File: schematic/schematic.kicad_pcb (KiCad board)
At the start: 2 copper layers, 53 parts, among them J1 USB_C_Receptacle_USB2.0, J2 Battery Connector, J3 Peltier Connection, SW1 SW_DIP_x01, U1 MC34063AD, U2 IRS2103, U3 MCP73832-2-OT, U4 BUK9K52-60E, U5 BUK9K52-60E, U6 IRS2103, U7 ESP32-D-WD-V3, Y1 Crystal_GND24

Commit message: schematic done
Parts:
- removed C9: 4.64pF, Capacitor_SMD:C_0805_2012Metric_Pad1.18x1.45mm_HandSolder
- added J4: Serial, Connector_PinHeader_2.54mm:PinHeader_1x03_P2.54mm_Vertical, F.Cu at (71.4, 97.7)
- added R20: 90k, Resistor_SMD:R_0805_2012Metric_Pad1.20x1.40mm_HandSolder, F.Cu at (94.0, 127.9)
- added R21: 90k, Resistor_SMD:R_0805_2012Metric_Pad1.20x1.40mm_HandSolder, F.Cu at (98.7, 124.9)
- added R24: 90k, Resistor_SMD:R_0805_2012Metric_Pad1.20x1.40mm_HandSolder, F.Cu at (103.5, 124.9)
- added TH1: SDNT2012X103F3950FTF, Resistor_SMD:R_0805_2012Metric_Pad1.20x1.40mm_HandSolder, F.Cu at (98.7, 130.8)
- added TH2: SDNT2012X103F3950FTF, Resistor_SMD:R_0805_2012Metric_Pad1.20x1.40mm_HandSolder, F.Cu at (103.5, 127.9)
- added TH3: SDNT2012X103F3950FTF, Resistor_SMD:R_0805_2012Metric_Pad1.20x1.40mm_HandSolder, F.Cu at (103.5, 130.8)
- C1: value 100pF -> 3.797pF
- C10: value 3.3nF -> 100nF; moved to B.Cu
- C11: value 10nF -> 10uF; moved to B.Cu
- C12: value 100nF -> 10uF; moved to B.Cu
- C13: value 10pF -> 10uF; moved to B.Cu
- C14, U4: moved to B.Cu
- C15: value 10pF -> 100pF; moved to B.Cu
- C16: value 100nF -> 100uF; footprint Capacitor_SMD:C_0805_2012Metric_Pad1.18x1.45mm_HandSolder -> Capacitor_SMD:C_1210_3225Metric_Pad1.33x2.70mm_HandSolder
- C18: value 100nF -> 1uF
- C2: value 100uF -> 4.64pF; footprint Capacitor_SMD:C_1206_3216Metric_Pad1.33x1.80mm_HandSolder -> Capacitor_SMD:C_0805_2012Metric_Pad1.18x1.45mm_HandSolder
- C3: value 10uF -> 3.3nF; moved to B.Cu
- C4: value 10uF -> 10nF; moved to B.Cu
- C5: value 1uF -> 100nF; moved to B.Cu
- C6: value 100nF -> 10pF; moved to B.Cu
- C7: value 10uF -> 10pF; moved to B.Cu
- C8: value 3.797pF -> 100nF
- D1, D2: value 1N5819 -> STPS130U; footprint Diode_THT:D_DO-41_SOD81_P10.16mm_Horizontal -> Diode_SMD:D_SMB; moved to B.Cu
- D3: value LED -> STPS130U; footprint Diode_THT:D_DO-41_SOD81_P10.16mm_Horizontal -> Diode_SMD:D_SMB
- D4: value 1N5819 -> LED; footprint Diode_THT:D_DO-41_SOD81_P10.16mm_Horizontal -> LED_SMD:LED_0805_2012Metric_Pad1.15x1.40mm_HandSolder; moved to B.Cu
- J1: value USB_C_Receptacle_USB2.0 -> Battery Connector; footprint 1KicadLib:USB4125-GF-A -> Connector_PinHeader_2.54mm:PinHeader_1x02_P2.54mm_Vertical
- J2: value Battery Connector -> USB_C_Receptacle_USB2.0; footprint Connector_PinHeader_2.54mm:PinHeader_1x02_P2.54mm_Vertical -> 1KicadLib:USB4125-GF-A
- L1: value 150uH -> 1.807nH; footprint Inductor_SMD:L_6.3x6.3_H3 -> Inductor_SMD:L_0805_2012Metric_Pad1.15x1.40mm_HandSolder
- L2: value 1.807nH -> 150uH; footprint Inductor_SMD:L_0805_2012Metric_Pad1.15x1.40mm_HandSolder -> Inductor_SMD:L_6.3x6.3_H3
- R1: value .22 -> 20k
- R10: value 470 -> .22; moved to B.Cu
- R11: value 10k -> 180
- R12: value 10k -> 500; moved to B.Cu
- R13: value 20k -> 3.6k; moved to B.Cu
- R14: value 10k -> 2.2k; moved to B.Cu
- R15: value 10k -> 470; moved to B.Cu
- R2, R3: value 0 -> 10k
- R4: value 180 -> 10k
- R5: value 5.1k -> 10k; footprint Capacitor_SMD:C_0805_2012Metric_Pad1.18x1.45mm_HandSolder -> Resistor_SMD:R_0805_2012Metric_Pad1.20x1.40mm_HandSolder
- R6: value 5.1k -> 76k; footprint Capacitor_SMD:C_0805_2012Metric_Pad1.18x1.45mm_HandSolder -> Resistor_SMD:R_0805_2012Metric_Pad1.20x1.40mm_HandSolder
- R7: value 3.6k -> 24k
- R8: value 2.2k -> 5.1k; footprint Resistor_SMD:R_0805_2012Metric_Pad1.20x1.40mm_HandSolder -> Capacitor_SMD:C_0805_2012Metric_Pad1.18x1.45mm_HandSolder; moved to B.Cu
- R9: value 2k -> 5.1k; footprint Resistor_SMD:R_0805_2012Metric_Pad1.20x1.40mm_HandSolder -> Capacitor_SMD:C_0805_2012Metric_Pad1.18x1.45mm_HandSolder; moved to B.Cu
- U1: value MC34063AD -> ESP32-D-WD-V3; footprint Package_SO:SOIC-8_3.9x4.9mm_P1.27mm -> Package_DFN_QFN:QFN-48-1EP_5x5mm_P0.35mm_EP3.7x3.7mm_ThermalVias
- U3: value MCP73832-2-OT -> BUK9K52-60E; footprint Package_TO_SOT_SMD:SOT-23-5 -> 1KicadLib:LFPAK56D; moved to B.Cu
- U5: value BUK9K52-60E -> IRS2103; footprint 1KicadLib:LFPAK56D -> Package_SO:SOIC-8_3.9x4.9mm_P1.27mm
- U6: value IRS2103 -> MC34063AD; moved to B.Cu
- U7: value ESP32-D-WD-V3 -> TP4054; footprint Package_DFN_QFN:QFN-48-1EP_5x5mm_P0.35mm_EP3.7x3.7mm_ThermalVias -> Package_TO_SOT_SMD:SOT-23-5_HandSoldering
- moved C3 68.1 mm to (79.6, 102.4), turned to 270 degrees
- moved C6 63.8 mm to (77.4, 98.8), turned to 180 degrees
- moved R12 63.3 mm to (82.2, 91.2), turned to 90 degrees
- moved R15 61.5 mm to (83.9, 90.9), turned to 270 degrees
- moved C10 60.5 mm to (80.9, 96.9), turned to 90 degrees
- moved R1 55.6 mm to (79.6, 102.3), turned to 270 degrees
- moved AE1 53.6 mm to (81.9, 117.1), turned to 270 degrees
- moved C5 52.8 mm to (83.2, 102.2)
- moved R11 52.5 mm to (88.4, 93.4), turned to 90 degrees
- moved R7 52.2 mm to (87.9, 102.5), turned to 270 degrees
- moved R8 51.8 mm to (94.3, 87.2), turned to 90 degrees
- moved R10 50.7 mm to (86.1, 94.7), turned to 270 degrees
- moved R14 50.2 mm to (90.3, 98.7)
- moved C7 49.3 mm to (77.2, 95.8)
- moved R13 49.2 mm to (87.1, 99.6), turned to 90 degrees
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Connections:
- C1 pad 1: Net-(C1-Pad1) -> Net-(AE1-Pad1)
- C10 pad 1: Net-(C10-Pad1) -> +3V3
- C10 pad 2: Net-(C10-Pad2) -> GND
- C11 pad 1: Net-(C10-Pad2) -> VCC_UNREGULATED
- C12 pad 1: +3V3 -> Net-(C12-Pad1)
- C12 pad 2: GND -> /Peltier Driver/PELTIER_P
- C13 pad 2: GND -> /Peltier Driver/PELTIER_N
- C14 pad 1: Net-(C14-Pad1) -> VCC_UNREGULATED
- C14 pad 2: Net-(C14-Pad2) -> GND
- C17 pad 1: +BATT -> +3V3
- C2 pad 1: +3V3 -> Net-(C2-Pad1)
- C3 pad 1: +BATT -> Net-(C3-Pad1)
- C3 pad 2: GND -> Net-(C3-Pad2)
- C4 pad 1: +3V3 -> Net-(C3-Pad2)
- C6 pad 1: +3V3 -> Net-(C6-Pad1)
- C7 pad 2: Net-(C7-Pad2) -> GND
- C8 pad 1: Net-(AE1-Pad1) -> +3V3
- D1 pad 1: Net-(D1-Pad1) -> Net-(C12-Pad1)
- D1 pad 2: GND -> VCC_UNREGULATED
- D2 pad 1: Net-(C7-Pad1) -> Net-(D2-Pad1)
- D2 pad 2: +BATT -> GND
- D3 pad 1: Net-(D3-Pad1) -> Net-(C13-Pad1)
- D3 pad 2: Net-(D3-Pad2) -> VCC_UNREGULATED
- D4 pad 1: Net-(C14-Pad1) -> Net-(D4-Pad1)
- D4 pad 2: +BATT -> Net-(D4-Pad2)
- J3 pad 1: Net-(C14-Pad2) -> /Peltier Driver/PELTIER_N
- J3 pad 2: Net-(C7-Pad2) -> /Peltier Driver/PELTIER_P
- L1 pad 1: +3V3 -> Net-(AE1-Pad1)
- L1 pad 2: Net-(D1-Pad1) -> Net-(C2-Pad1)
- L2 pad 1: Net-(AE1-Pad1) -> +3V3
- L2 pad 2: Net-(C9-Pad1) -> Net-(D2-Pad1)
- R1 pad 1: Net-(R1-Pad1) -> Net-(C3-Pad1)
- R1 pad 2: +BATT -> Net-(C3-Pad2)
- R10 pad 1: VBUS -> Net-(R10-Pad1)
- R10 pad 2: Net-(D3-Pad2) -> VCC_UNREGULATED
- R11 pad 1: Net-(R11-Pad1) -> Net-(R10-Pad1)
- R12 pad 1: Net-(R12-Pad1) -> GND
- R13 pad 1: Net-(C10-Pad1) -> +3V3
- R13 pad 2: Net-(C10-Pad2) -> Net-(R13-Pad2)
- R14 pad 1: Net-(R14-Pad1) -> Net-(R13-Pad2)
- R14 pad 2: Net-(R14-Pad2) -> GND
- R15 pad 1: Net-(R15-Pad1) -> VBUS
- R15 pad 2: Net-(R15-Pad2) -> Net-(D4-Pad2)
- R2 pad 1: Net-(J1-PadA6) -> Net-(R2-Pad1)
- R2 pad 2: TXD -> Net-(R2-Pad2)
- R3 pad 1: Net-(J1-PadA7) -> Net-(R3-Pad1)
- R3 pad 2: RXD -> Net-(R3-Pad2)
- R4 pad 1: Net-(R1-Pad1) -> Net-(R4-Pad1)
- R5 pad 1: Net-(J1-PadB5) -> Net-(R5-Pad1)
- R5 pad 2: GND -> Net-(R5-Pad2)
- R6 pad 1: Net-(J1-PadA5) -> VCC_UNREGULATED
- R6 pad 2: GND -> Net-(R6-Pad2)
- R7 pad 1: +3V3 -> Net-(R6-Pad2)
- R7 pad 2: Net-(R7-Pad2) -> GND
- R8 pad 1: Net-(R7-Pad2) -> Net-(J2-PadB5)
- R9 pad 1: GND -> Net-(J2-PadA5)
- R9 pad 2: Net-(R9-Pad2) -> GND
- SW1 pad 1: Net-(J2-Pad1) -> VCC_UNREGULATED
- SW1 pad 2: +BATT -> /Power Management/BATT_IN
- U1 pad 1: Net-(R1-Pad1) -> +3V3
- U1 pad 2: Net-(D1-Pad1) -> Net-(C2-Pad1)
- U1 pad 3: Net-(C1-Pad1) -> +3V3
- U1 pad 4: GND -> +3V3
- U1 pad 5: Net-(R7-Pad2) -> Net-(U1-Pad5)
- U1 pad 6: +BATT -> Net-(U1-Pad6)
- U1 pad 7: Net-(R1-Pad1) -> Net-(U1-Pad7)
- U1 pad 8: Net-(R4-Pad2) -> Net-(U1-Pad8)
- U2 pad 1: +BATT -> VCC_UNREGULATED
- U2 pad 2: HBridgeA -> DRIVER_P
- U2 pad 3: HBridgeA -> DRIVER_P
- U2 pad 5: Net-(R12-Pad2) -> Net-(R3-Pad2)
- U2 pad 6: Net-(C7-Pad2) -> /Peltier Driver/PELTIER_P
- U2 pad 7: Net-(R11-Pad2) -> Net-(R2-Pad2)
- U2 pad 8: Net-(C7-Pad1) -> Net-(C12-Pad1)
- U3 pad 1: Net-(D3-Pad1) -> /Peltier Driver/PELTIER_P
- U3 pad 2: GND -> Net-(R2-Pad1)
- U3 pad 3: Net-(J2-Pad1) -> GND
- U3 pad 4: VBUS -> Net-(R3-Pad1)
- U3 pad 5: Net-(R9-Pad2) -> /Peltier Driver/PELTIER_P
- U4 pad 1: Net-(C7-Pad2) -> /Peltier Driver/PELTIER_N
- U4 pad 2: Net-(R11-Pad1) -> Net-(R4-Pad1)
- U4 pad 4: Net-(R12-Pad1) -> Net-(R5-Pad1)
- U4 pad 5: Net-(C7-Pad2) -> /Peltier Driver/PELTIER_N
- U4 pad 6: Net-(C7-Pad2) -> /Peltier Driver/PELTIER_N
- U4 pad 7: +BATT -> VCC_UNREGULATED
- U4 pad 8: +BATT -> VCC_UNREGULATED
- U5 pad 1: Net-(C14-Pad2) -> VCC_UNREGULATED
- U5 pad 2: Net-(R14-Pad1) -> DRIVER_N
- U5 pad 3: GND -> DRIVER_N
- U5 pad 4: Net-(R15-Pad1) -> GND
- U5 pad 5: Net-(C14-Pad2) -> Net-(R5-Pad2)
- U5 pad 6: Net-(C14-Pad2) -> /Peltier Driver/PELTIER_N
- U5 pad 7: +BATT -> Net-(R4-Pad2)
- U5 pad 8: +BATT -> Net-(C13-Pad1)
- U6 pad 1: +BATT -> Net-(R10-Pad1)
- U6 pad 2: HBridgeB -> Net-(D2-Pad1)
- U6 pad 3: HBridgeB -> Net-(C15-Pad1)
- U6 pad 5: Net-(R15-Pad2) -> Net-(R13-Pad2)
- U6 pad 6: Net-(C14-Pad2) -> VCC_UNREGULATED
- U6 pad 7: Net-(R14-Pad2) -> Net-(R10-Pad1)
- U6 pad 8: Net-(C14-Pad1) -> Net-(R11-Pad2)
- U7 pad 1: +3V3 -> Net-(D4-Pad1)
- U7 pad 2: Net-(C9-Pad1) -> GND
- U7 pad 3: +3V3 -> /Power Management/BATT_IN
- U7 pad 4: +3V3 -> VBUS
- U7 pad 5: Net-(U7-Pad5) -> Net-(R12-Pad2)
- Y1 pad 1: Net-(C13-Pad1) -> Net-(C6-Pad1)
- Y1 pad 3: Net-(C15-Pad1) -> Net-(C7-Pad1)
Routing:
- net VCC_UNREGULATED: track 0.00 -> 81.1 mm, vias 0 -> 6
- net DRIVER_P: track 0.00 -> 48.3 mm, vias 0 -> 2
- net +3V3: track 0.00 -> 42.8 mm, vias 0 -> 5
- net DRIVER_N: track 0.00 -> 31.9 mm
- net /Peltier Driver/PELTIER_P: track 0.00 -> 31.4 mm, vias 0 -> 1
- net /Power Management/BATT_IN: track 0.00 -> 24.6 mm
- net /Peltier Driver/PELTIER_N: track 0.00 -> 23.7 mm, vias 0 -> 1
- net VBUS: track 0.00 -> 15.4 mm, vias 0 -> 2
- net GND: track 0.00 -> 11.8 mm, vias 0 -> 8
- net Net-(C2-Pad1): track 0.00 -> 8.32 mm
- net Net-(C7-Pad1): track 0.00 -> 8.06 mm, vias 0 -> 1
- net Net-(C12-Pad1): track 0.00 -> 8.04 mm, vias 0 -> 1
- net Net-(R10-Pad1): track 0.00 -> 7.81 mm, vias 0 -> 1
- net Net-(C13-Pad1): track 0.00 -> 7.33 mm, vias 0 -> 1
- net Net-(D2-Pad1): track 0.00 -> 5.75 mm
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- added copper zone on B.Cu, net GND
- added copper zone on F.Cu, net GND
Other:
- net class Default: clearance 0.2 -> 0.127; trace_width 0.25 -> 0.127; via_dia 0.8 -> 0.4; via_drill 0.4 -> 0.2
- rule trace_clearance: 0.2 -> 0.127
- rule trace_min: 0.2 -> 0.127
- rule via_min_drill: 0.3 -> 0.2

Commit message: nightly
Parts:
- removed J1: Battery Connector, Connector_PinHeader_2.54mm:PinHeader_1x02_P2.54mm_Vertical
- added Je: BATT, Connector_PinHeader_1.27mm:PinHeader_1x02_P1.27mm_Vertical, F.Cu at (137.4, 64.3)
- J3: value Peltier Connection -> Pelt; footprint Connector_PinHeader_2.54mm:PinHeader_1x02_P2.54mm_Vertical -> Connector_PinHeader_1.27mm:PinHeader_1x02_P1.27mm_Vertical
- J4: footprint Connector_PinHeader_2.54mm:PinHeader_1x03_P2.54mm_Vertical -> Connector_PinHeader_1.27mm:PinHeader_1x03_P1.27mm_Vertical
- SW1: value SW_DIP_x01 -> PS; footprint Connector_PinHeader_2.54mm:PinHeader_1x02_P2.54mm_Vertical -> Connector_PinHeader_1.27mm:PinHeader_1x02_P1.27mm_Vertical
- moved AE1 75.8 mm to (154.7, 95.8)
- moved C1 73.8 mm to (153.5, 91.9), turned to 45 degrees
- moved L1 71.9 mm to (150.9, 90.6), turned to 135 degrees
- moved C2 67.7 mm to (148.1, 89.3), turned to 225 degrees
- moved J4 67.2 mm to (137.3, 84.7), turned to 90 degrees
- moved SW1 64.6 mm to (137.3, 69.2)
- moved J3 64.4 mm to (172.6, 71.1)
- moved C4 64.1 mm to (138.0, 81.0)
- moved R13 64.1 mm to (147.6, 78.2)
- moved C7 64.1 mm to (137.7, 74.4)
- moved C8 64.1 mm to (148.3, 77.3)
- moved L2 64.1 mm to (153.5, 75.4)
- moved R12 64.1 mm to (142.6, 69.8)
- moved R3 64.1 mm to (164.1, 63.6)
- moved R6 64.1 mm to (150.2, 81.1)
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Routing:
- net +3V3: track 42.8 -> 138.6 mm, vias 5 -> 7
- net GND: track 11.8 -> 102.3 mm, vias 8 -> 28
- net TEMP_SENSE_3: track 0.00 -> 63.8 mm, vias 0 -> 2
- net TEMP_SENSE_2: track 0.00 -> 44.8 mm, vias 0 -> 2
- net TEMP_SENSE_1: track 0.00 -> 31.6 mm, vias 0 -> 2
- net RXD: track 0.00 -> 10.8 mm
- net TXD: track 0.00 -> 9.84 mm
- net /Power Management/BATT_IN: track 24.6 -> 17.1 mm, vias 0 -> 1
- net Net-(C2-Pad1): track 8.32 -> 13.0 mm
- net DRIVER_N: track 31.9 -> 34.9 mm
- net /Peltier Driver/PELTIER_N: track 23.7 -> 24.8 mm
- net DRIVER_P: track 48.3 -> 49.2 mm
- net Net-(AE1-Pad1): track 3.79 -> 4.48 mm
- net VCC_UNREGULATED: track 81.1 -> 80.6 mm
- net Net-(C7-Pad1): track 8.06 -> 7.82 mm, vias 1 -> 2
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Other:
- board outline added: 40.6 x 70.5 mm
- board text added: "GUANTANAMO BAY"
- board text added: "Joesphan Lu"

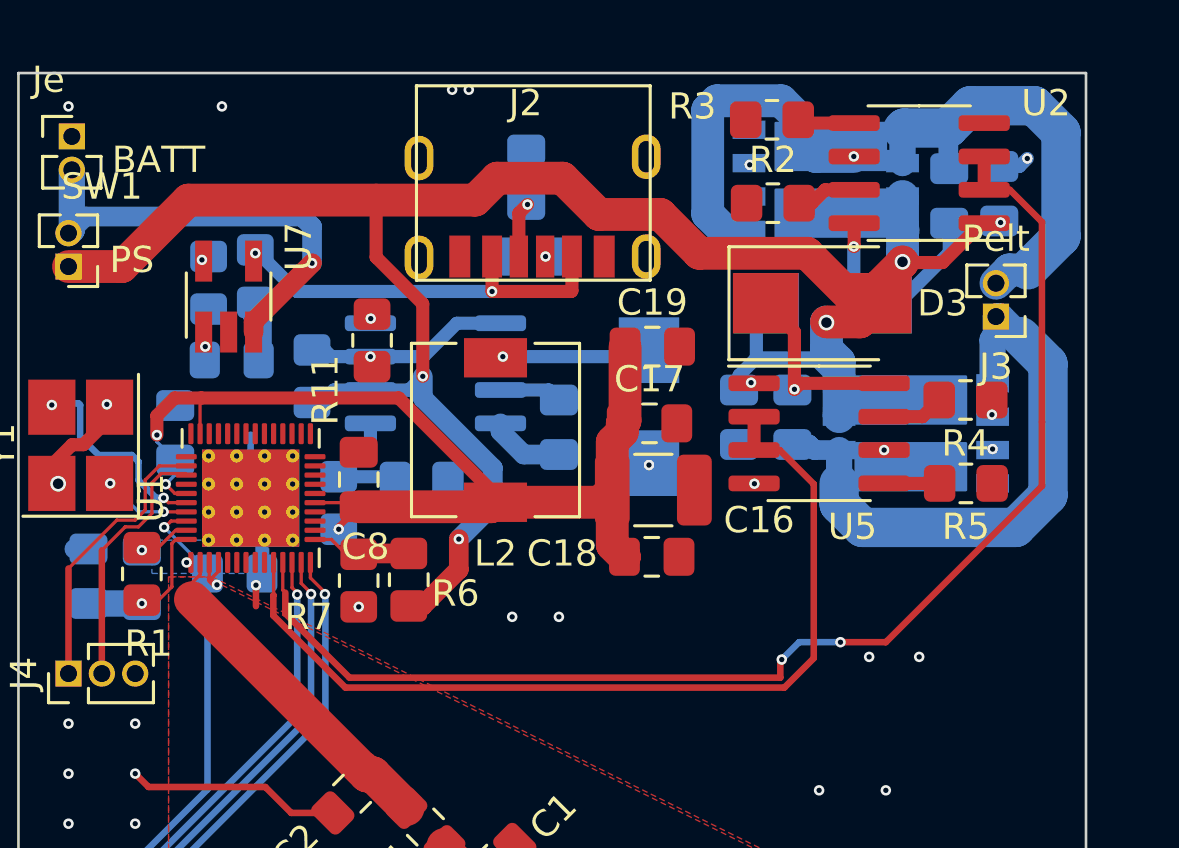
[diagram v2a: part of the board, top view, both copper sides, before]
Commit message: fixed vias
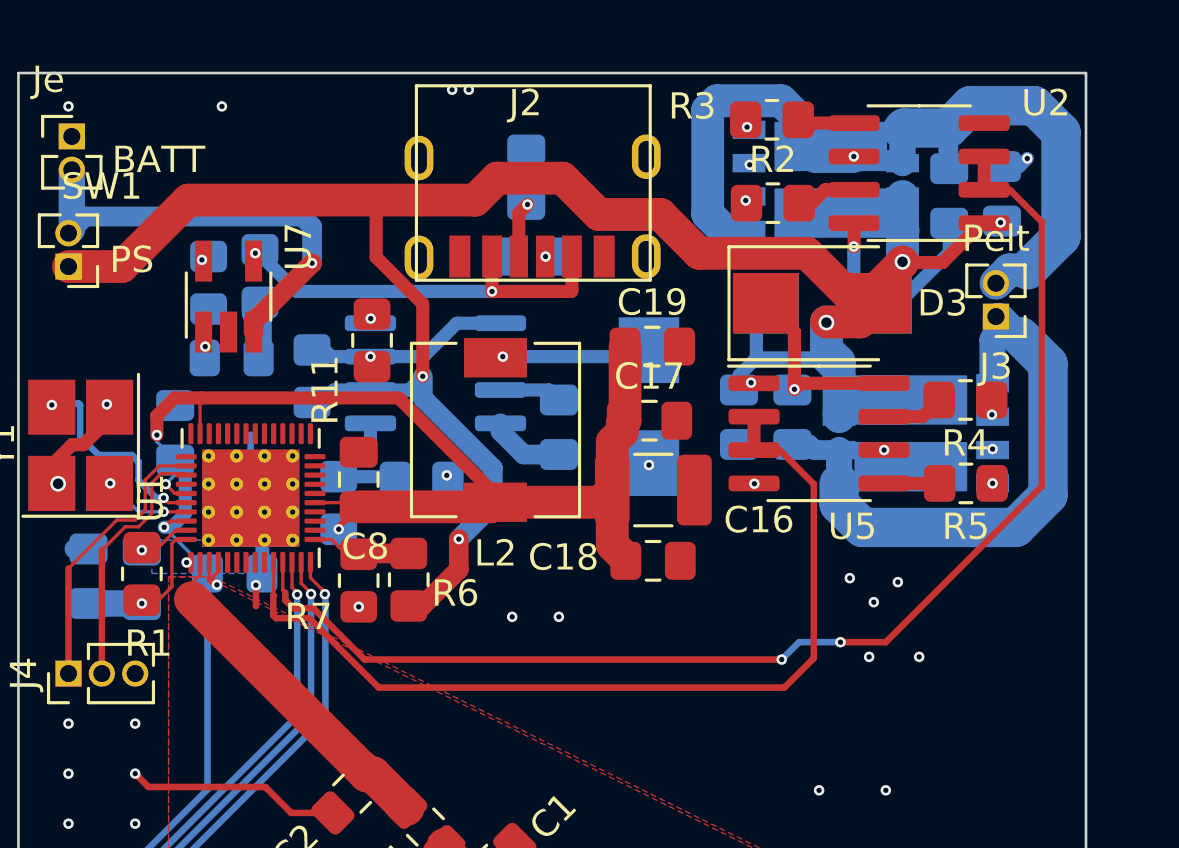
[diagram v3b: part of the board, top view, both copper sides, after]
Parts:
- moved R15 0.18 mm to (144.6, 69.6)
- moved C18 0.16 mm to (159.5, 80.4)
- moved C11 0.10 mm to (172.8, 66.4)
- moved C17 0.10 mm to (159.4, 75.1)
- moved D4 0.08 mm to (143.5, 72.7)
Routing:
- net +3V3: track 138.6 -> 141.9 mm
- net DRIVER_P: track 49.2 -> 48.0 mm
- net Net-(R5-Pad1): vias 0 -> 1
- net Net-(R3-Pad1): vias 0 -> 1
- net Net-(R2-Pad1): vias 0 -> 1
- net GND: vias 28 -> 32

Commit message: final winter qtr push
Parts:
- removed C12, C13, C14: 10uF, Capacitor_SMD:C_0805_2012Metric_Pad1.18x1.45mm_HandSolder
- removed C19: 100nF, Capacitor_SMD:C_0805_2012Metric_Pad1.18x1.45mm_HandSolder
- removed D3: STPS130U, Diode_SMD:D_SMB
- removed Je: BATT, Connector_PinHeader_1.27mm:PinHeader_1x02_P1.27mm_Vertical
- removed R4, R5: 10k, Resistor_SMD:R_0805_2012Metric_Pad1.20x1.40mm_HandSolder
- removed R6: 76k, Resistor_SMD:R_0805_2012Metric_Pad1.20x1.40mm_HandSolder
- removed R7: 24k, Resistor_SMD:R_0805_2012Metric_Pad1.20x1.40mm_HandSolder
- removed U5: IRS2103, Package_SO:SOIC-8_3.9x4.9mm_P1.27mm
- added BT1: Battery_Cell, Connector_PinHeader_2.54mm:PinHeader_1x02_P2.54mm_Vertical, F.Cu at (117.3, 99.0)
- added BT2: Battery_Cell, Connector_PinHeader_2.54mm:PinHeader_1x02_P2.54mm_Vertical, F.Cu at (117.3, 106.7)
- added BT3: Battery_Cell, Connector_PinHeader_2.54mm:PinHeader_1x02_P2.54mm_Vertical, F.Cu at (117.3, 114.2)
- added C20: Cfw (DNP), Capacitor_SMD:C_0805_2012Metric_Pad1.18x1.45mm_HandSolder, F.Cu at (140.7, 104.6)
- added C21: 100nF, Capacitor_SMD:C_0805_2012Metric_Pad1.18x1.45mm_HandSolder, B.Cu at (132.6, 100.2)
- added C9: 10uF, Capacitor_SMD:C_0805_2012Metric_Pad1.18x1.45mm_HandSolder, F.Cu at (131.4, 82.9)
- added L3: 33uH, Inductor_SMD:L_12x12mm_H4.5mm, B.Cu at (137.8, 91.4)
- added R16: 28.7, Resistor_SMD:R_2512_6332Metric_Pad1.40x3.35mm_HandSolder, F.Cu at (121.2, 114.5)
- added R17: 200, Resistor_SMD:R_0805_2012Metric_Pad1.20x1.40mm_HandSolder, B.Cu at (132.7, 103.2)
- added R18: 200, Resistor_SMD:R_0805_2012Metric_Pad1.20x1.40mm_HandSolder, F.Cu at (130.8, 107.4)
- added R19: 200, Resistor_SMD:R_0805_2012Metric_Pad1.20x1.40mm_HandSolder, F.Cu at (130.8, 112.4)
- added R22: 100k, Resistor_SMD:R_0805_2012Metric_Pad1.20x1.40mm_HandSolder, F.Cu at (125.2, 102.6)
- added R23: 22k, Resistor_SMD:R_0805_2012Metric_Pad1.20x1.40mm_HandSolder, F.Cu at (127.0, 104.6)
- added R25: 390, Resistor_SMD:R_0805_2012Metric_Pad1.20x1.40mm_HandSolder, F.Cu at (127.9, 107.5)
- added R26: 180k, Resistor_SMD:R_0805_2012Metric_Pad1.20x1.40mm_HandSolder, F.Cu at (125.1, 108.4)
- added R27: 68k, Resistor_SMD:R_0805_2012Metric_Pad1.20x1.40mm_HandSolder, F.Cu at (126.9, 111.4)
- added R28: 56k, Resistor_SMD:R_0805_2012Metric_Pad1.20x1.40mm_HandSolder, F.Cu at (124.1, 113.5)
- added R29: 68k, Resistor_SMD:R_0805_2012Metric_Pad1.20x1.40mm_HandSolder, F.Cu at (124.1, 117.3)
- added R30: 220k, Resistor_SMD:R_0805_2012Metric_Pad1.20x1.40mm_HandSolder, F.Cu at (125.8, 99.3)
- added R31: 56k, Resistor_SMD:R_0805_2012Metric_Pad1.20x1.40mm_HandSolder, B.Cu at (126.6, 90.3)
- added R32: 120, Resistor_SMD:R_0805_2012Metric_Pad1.20x1.40mm_HandSolder, B.Cu at (122.8, 90.3)
- added R33: 500, Resistor_SMD:R_0805_2012Metric_Pad1.20x1.40mm_HandSolder, B.Cu at (127.2, 93.2)
- added R34: .1, Resistor_SMD:R_1206_3216Metric_Pad1.30x1.75mm_HandSolder, F.Cu at (128.3, 86.7)
- added R35: 1k, Resistor_SMD:R_0805_2012Metric_Pad1.20x1.40mm_HandSolder, B.Cu at (129.0, 98.4)
- added R36: 1k, Resistor_SMD:R_0805_2012Metric_Pad1.20x1.40mm_HandSolder, B.Cu at (129.6, 91.3)
- added R37: 12.5k, Resistor_SMD:R_0805_2012Metric_Pad1.20x1.40mm_HandSolder, B.Cu at (126.3, 96.1)
- added R38: 12.5k, Resistor_SMD:R_0805_2012Metric_Pad1.20x1.40mm_HandSolder, B.Cu at (129.5, 95.2)
- added R39: 150k, Resistor_SMD:R_0805_2012Metric_Pad1.20x1.40mm_HandSolder, F.Cu at (135.5, 115.2)
- added R40: 100k, Resistor_SMD:R_0805_2012Metric_Pad1.20x1.40mm_HandSolder, F.Cu at (135.5, 111.1)
- added U10: BSD316, Package_TO_SOT_SMD:SOT-363_SC-70-6_Handsoldering, F.Cu at (121.6, 108.7)
- added U11: BSD316, Package_TO_SOT_SMD:SOT-363_SC-70-6_Handsoldering, B.Cu at (121.6, 117.2)
- added U12: PC817, Package_SO:SOP-4_3.8x4.1mm_P2.54mm, B.Cu at (127.0, 103.9)
- added U13: PC817, Package_SO:SOP-4_3.8x4.1mm_P2.54mm, B.Cu at (126.9, 108.6)
- added U14: PC817, Package_SO:SOP-4_3.8x4.1mm_P2.54mm, B.Cu at (126.9, 113.4)
- added U15: AS431, Package_TO_SOT_SMD:SOT-23-5_HandSoldering, B.Cu at (123.7, 93.2)
- added U16: LM324, Package_SO:SOIC-14_3.9x8.7mm_P1.27mm, F.Cu at (127.0, 92.7)
- added U17: XL6009, Package_TO_SOT_SMD:TO-263-5_TabPin3, F.Cu at (139.2, 90.9)
- added U18: PAM2305CGFADJ, Package_DFN_QFN:DFN-6-1EP_2x2mm_P0.65mm_EP1x1.6mm, F.Cu at (145.2, 106.4)
- added U8: PC817, Package_SO:SOP-4_3.8x4.1mm_P2.54mm, B.Cu at (132.1, 79.0)
- added U9: BSD316, Package_TO_SOT_SMD:SOT-363_SC-70-6_Handsoldering, B.Cu at (121.2, 102.7)
- C1, C17, C18, C2, C8, R1, R20, TH2, TH3, Y1: moved to B.Cu
- C10, C3, C5, U3, U4: moved to F.Cu
- C15: value 100pF -> 10uF
- D1: value STPS130U -> LL4148; footprint Diode_SMD:D_SMB -> Diode_SMD:D_MiniMELF; moved to F.Cu
- D2: value STPS130U -> LL4148; footprint Diode_SMD:D_SMB -> Diode_SMD:D_MiniMELF
- D4: value LED -> SS34; footprint LED_SMD:LED_0805_2012Metric_Pad1.15x1.40mm_HandSolder -> Diode_SMD:D_SMC_Handsoldering; moved to F.Cu
- J3: value Pelt -> Peltier Connection; footprint Connector_PinHeader_1.27mm:PinHeader_1x02_P1.27mm_Vertical -> Connector_PinHeader_2.54mm:PinHeader_1x02_P2.54mm_Vertical
- J4: footprint Connector_PinHeader_1.27mm:PinHeader_1x03_P1.27mm_Vertical -> Connector_PinHeader_2.54mm:PinHeader_1x03_P2.54mm_Vertical
- L2: value 150uH -> 10uH NR8040T100M; footprint Inductor_SMD:L_6.3x6.3_H3 -> Inductor_SMD:L_Taiyo-Yuden_NR-80xx_HandSoldering; moved to B.Cu
- R10: value .22 -> 300; moved to F.Cu
- R11: value 180 -> 300
- R12: value 500 -> 28.7; footprint Resistor_SMD:R_0805_2012Metric_Pad1.20x1.40mm_HandSolder -> Resistor_SMD:R_2512_6332Metric_Pad1.40x3.35mm_HandSolder; moved to F.Cu
- R13: value 3.6k -> 33k; moved to F.Cu
- R14: value 2.2k -> 7.5k; moved to F.Cu
- R15: value 470 -> 28.7; footprint Resistor_SMD:R_0805_2012Metric_Pad1.20x1.40mm_HandSolder -> Resistor_SMD:R_2512_6332Metric_Pad1.40x3.35mm_HandSolder
- R2, R3: value 10k -> 300
- SW1: value PS -> Power Switch; footprint Connector_PinHeader_1.27mm:PinHeader_1x02_P1.27mm_Vertical -> Connector_PinHeader_2.54mm:PinHeader_1x02_P2.54mm_Vertical
- U1: footprint Package_DFN_QFN:QFN-48-1EP_5x5mm_P0.35mm_EP3.7x3.7mm_ThermalVias -> Package_DFN_QFN:QFN-48-1EP_5x5mm_P0.35mm_EP3.7x3.7mm
- U2: value IRS2103 -> PC817; footprint Package_SO:SOIC-8_3.9x4.9mm_P1.27mm -> Package_SO:SOP-4_3.8x4.1mm_P2.54mm; moved to B.Cu
- U6: value MC34063AD -> PC817; footprint Package_SO:SOIC-8_3.9x4.9mm_P1.27mm -> Package_SO:SOP-4_3.8x4.1mm_P2.54mm
- U7: value TP4054 -> PC817; footprint Package_TO_SOT_SMD:SOT-23-5_HandSoldering -> Package_SO:SOP-4_3.8x4.1mm_P2.54mm; moved to B.Cu
- moved TH1 47.7 mm to (179.1, 76.5)
- moved R20 46.3 mm to (179.1, 76.5)
- moved R15 46.1 mm to (121.1, 109.2)
- moved C7 42.1 mm to (139.5, 116.5), turned to 180 degrees
- moved C10 40.8 mm to (137.7, 116.2), turned to -90 degrees
- moved U4 40.5 mm to (130.6, 79.8)
- moved C6 39.4 mm to (143.3, 116.5), turned to 0 degrees
- moved C17 38.6 mm to (135.8, 105.7), turned to -90 degrees
- moved R12 37.9 mm to (121.2, 101.1), turned to -90 degrees
- moved R1 37.8 mm to (144.3, 118.5), turned to 0 degrees
- moved Y1 37.4 mm to (141.9, 113.1), turned to 180 degrees
- moved R8 37.2 mm to (120.9, 81.3), turned to 180 degrees
- moved C16 36.5 mm to (136.2, 105.8), turned to 180 degrees
- moved C3 36.3 mm to (144.4, 117.1), turned to 0 degrees
- moved TH3 36.1 mm to (152.5, 94.1)
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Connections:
- AE1 pad 2: Net-(AE1-Pad2) -> unconnected-(AE1-Pad2)
- C11 pad 1: VCC_UNREGULATED -> Vdrive
- C15 pad 1: Net-(C15-Pad1) -> +BATT
- D1 pad 1: Net-(C12-Pad1) -> Net-(C9-Pad1)
- D2 pad 1: Net-(D2-Pad1) -> Vdrive
- D2 pad 2: GND -> Net-(C9-Pad1)
- D4 pad 1: Net-(D4-Pad1) -> +BATT
- J2 pad A9: VBUS -> USB_PWR
- J2 pad B9: VBUS -> USB_PWR
- L2 pad 2: Net-(D2-Pad1) -> Net-(L2-Pad2)
- R10 pad 2: VCC_UNREGULATED -> DRIVER_N
- R11 pad 1: Net-(R10-Pad1) -> Net-(R11-Pad1)
- R11 pad 2: Net-(R11-Pad2) -> DRIVER_P
- R12 pad 1: GND -> +BATT
- R15 pad 1: VBUS -> Net-(BT1-Pad2)
- R15 pad 2: Net-(D4-Pad2) -> Net-(R15-Pad2)
- R2 pad 2: Net-(R2-Pad2) -> DRIVER_P
- R3 pad 2: Net-(R3-Pad2) -> DRIVER_N
- SW1 pad 2: /Power Management/BATT_IN -> +BATT
- U1 pad 15: Net-(R6-Pad2) -> unconnected-(U1-Pad15)
- U1 pad 16: Net-(U1-Pad16) -> PWM
- U1 pad 17: Net-(U1-Pad17) -> unconnected-(U1-Pad17)
- U1 pad 18: Net-(U1-Pad18) -> unconnected-(U1-Pad18)
- U1 pad 20: Net-(U1-Pad20) -> unconnected-(U1-Pad20)
- U1 pad 21: Net-(U1-Pad21) -> unconnected-(U1-Pad21)
- U1 pad 22: Net-(U1-Pad22) -> CELL_MEAS_3
- U1 pad 23: Net-(U1-Pad23) -> CELL_MEAS_2
- U1 pad 24: Net-(U1-Pad24) -> CELL_MEAS_1
- U1 pad 25: Net-(U1-Pad25) -> CELL_DSCHG_3
- U1 pad 26: Net-(U1-Pad26) -> unconnected-(U1-Pad26)
- U1 pad 27: Net-(U1-Pad27) -> CELL_DSCHG_2
- U1 pad 28: Net-(U1-Pad28) -> unconnected-(U1-Pad28)
- U1 pad 29: Net-(U1-Pad29) -> unconnected-(U1-Pad29)
- U1 pad 30: Net-(U1-Pad30) -> unconnected-(U1-Pad30)
- U1 pad 31: Net-(U1-Pad31) -> unconnected-(U1-Pad31)
- U1 pad 32: Net-(U1-Pad32) -> unconnected-(U1-Pad32)
- U1 pad 33: Net-(U1-Pad33) -> unconnected-(U1-Pad33)
- U1 pad 34: Net-(U1-Pad34) -> CELL_DSCHG_1
- U1 pad 36: Net-(U1-Pad36) -> unconnected-(U1-Pad36)
- U1 pad 38: Net-(U1-Pad38) -> unconnected-(U1-Pad38)
- U1 pad 39: Net-(U1-Pad39) -> unconnected-(U1-Pad39)
- U1 pad 42: Net-(U1-Pad42) -> unconnected-(U1-Pad42)
- U1 pad 5: Net-(U1-Pad5) -> unconnected-(U1-Pad5)
- U1 pad 6: Net-(U1-Pad6) -> unconnected-(U1-Pad6)
- U1 pad 7: Net-(U1-Pad7) -> unconnected-(U1-Pad7)
- U1 pad 8: Net-(U1-Pad8) -> unconnected-(U1-Pad8)
- U1 pad 9: Net-(U1-Pad9) -> unconnected-(U1-Pad9)
- U2 pad 1: VCC_UNREGULATED -> Net-(R2-Pad1)
- U2 pad 2: DRIVER_P -> GND
- U2 pad 3: DRIVER_P -> Net-(U3-Pad2)
- U2 pad 4: GND -> unconnected-(U2-Pad4)
- U3 pad 2: Net-(R2-Pad1) -> Net-(U3-Pad2)
- U3 pad 4: Net-(R3-Pad1) -> Net-(U3-Pad4)
- U4 pad 2: Net-(R4-Pad1) -> Net-(U4-Pad2)
- U6 pad 1: Net-(R10-Pad1) -> Net-(R3-Pad1)
- U6 pad 2: Net-(D2-Pad1) -> GND
- U6 pad 3: Net-(C15-Pad1) -> Net-(U3-Pad4)
- U6 pad 4: GND -> Vdrive
- U7 pad 1: Net-(D4-Pad1) -> Net-(R10-Pad1)
- U7 pad 3: /Power Management/BATT_IN -> Net-(U4-Pad2)
- U7 pad 4: VBUS -> Vdrive
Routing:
- net GND: track 102.3 -> 3.18 mm, vias 32 -> 21
- net USB_PWR: track 0.00 -> 54.7 mm, vias 0 -> 10
- net PWM: track 0.00 -> 44.9 mm, vias 0 -> 2
- net TEMP_SENSE_3: track 63.8 -> 22.9 mm
- net Vdrive: track 0.00 -> 39.5 mm
- net +BATT: track 0.00 -> 29.5 mm, vias 0 -> 4
- net DRIVER_N: track 34.9 -> 61.0 mm, vias 0 -> 2
- net /Peltier Driver/PELTIER_P: track 31.6 -> 6.37 mm, vias 1 -> 2
- net CELL_MEAS_3: track 0.00 -> 24.7 mm, vias 0 -> 2
- net +3V3: track 141.9 -> 117.4 mm, vias 7 -> 10
- net Net-(R34-Pad1): track 0.00 -> 21.5 mm, vias 0 -> 1
- net TEMP_SENSE_1: track 31.6 -> 52.7 mm
- net CELL_MEAS_1: track 0.00 -> 20.6 mm, vias 0 -> 2
- net VCC_UNREGULATED: track 80.6 -> 101.2 mm, vias 6 -> 2
- net CELL_MEAS_2: track 0.00 -> 19.0 mm, vias 0 -> 2
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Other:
- board size 40.6 x 70.5 mm -> 67.3 x 52.1 mm
- net class Default removed

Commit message: a
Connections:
- net USB_PWR renamed VBUS
- U2 pad 4: unconnected-(U2-Pad4) -> Vdrive
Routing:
- net Vdrive: track 39.5 -> 40.9 mm

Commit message: E
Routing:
- net GND: vias 21 -> 23
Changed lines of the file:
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@@
   (via (at 142.651 112.63) (size 0.4) (drill 0.2) (layers "F.Cu" "B.Cu") (net 3))
   (via (at 148.8948 73.6854) (size 0.4) (drill 0.2) (layers "F.Cu" "B.Cu") (free) (net 3))
+  (via (at 134.5438 105.5878) (size 0.4) (drill 0.2) (layers "F.Cu" "B.Cu") (net 3))
   (via (at 143.159 112.122) (size 0.4) (drill 0.2) (layers "F.Cu" "B.Cu") (net 3))
   (via (at 170.18 71.12) (size 0.4) (drill 0.2) (layers "F.Cu" "B.Cu") (free) (net 3))
@@
   (via (at 156.21 83.82) (size 0.4) (drill 0.2) (layers "F.Cu" "B.Cu") (free) (net 3))
   (via (at 162.56 72.39) (size 0.4) (drill 0.2) (layers "F.Cu" "B.Cu") (free) (net 3))
+  (via (at 135.2296 106.68) (size 0.4) (drill 0.2) (layers "F.Cu" "B.Cu") (net 3))
   (segment (start 145.191 109.6074) (end 145.191 110.242) (width 0.5) (layer "B.Cu") (net 3))
   (segment (start 145.191 110.242) (end 143.392 112.041) (width 0.5) (layer "B.Cu") (net 3))
